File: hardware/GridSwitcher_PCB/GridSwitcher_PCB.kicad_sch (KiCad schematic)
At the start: 32 parts, among them IC5 ESDS304DBVR, IC8 ESDS304DBVR, IC9 ESDS304DBVR, J10 RS485, J11 Relays, J12 LEDs, J9 Display and Keypad, U1 74LS09, U2 74LS09, U33 SN65HVD11HD

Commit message: -enh made some progress on pcb/fp design
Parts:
- removed J10: RS485, symbol Connector:4P4C_Shielded
- removed J11: Relays, symbol Connector:Conn_01x16_Pin
- added J10: Temp Sensor RS485, Connector_JST:JST_PH_B4B-PH-K_1x04_P2.00mm_Vertical, symbol Connector:Conn_01x04_Pin
- added J13: UT_OUT, Connector_Dsub:DSUB-25_Female_Horizontal_P2.77x2.84mm_EdgePinOffset7.70mm_Housed_MountingHolesOffset9.12mm, symbol Connector:DB25_Plug_MountingHoles
- added R111, R112: DNP, Resistor_SMD:R_0603_1608Metric_Pad0.98x0.95mm_HandSolder, symbol Device:R
- H1: footprint (none) -> MountingHole:MountingHole_3.2mm_M3_ISO14580_Pad_TopBottom
- IC5, IC8, IC9: footprint (none) -> Library:SOT95P280X145-5N
- J5: renamed from J9; footprint (none) -> Connector_JST:JST_PHD_B12B-PHDSS_2x06_P2.00mm_Vertical
- J6: renamed from J12; footprint (none) -> Connector_JST:JST_PH_B6B-PH-K_1x06_P2.00mm_Vertical
- R103, R104, R105, R106, R2, R3, R4, R5, R81, R82, R83, R84, R85, R86, R87, R88, R89, R90, R91, R92: footprint (none) -> Resistor_SMD:R_0603_1608Metric_Pad0.98x0.95mm_HandSolder
- U1, U2: footprint (none) -> Package_SO:SO-14_5.3x10.2mm_P1.27mm
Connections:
- net +3V3: now also R112.2
- net +5V: now also R111.1
- net GND: now also J10.1 (Pin_1), J13.0 (PAD), J13.1, J13.13, J13.14 (P14), J13.16 (P16), J13.25 (P25), J13.3, J13.4
- net mosfet_drivers/MOS_10_OUT: now also J13.20 (P20)
- net mosfet_drivers/MOS_11_OUT: now also J13.7
- net mosfet_drivers/MOS_12_OUT: now also J13.19 (P19)
- net mosfet_drivers/MOS_13_OUT: now also J13.6
- net mosfet_drivers/MOS_14_OUT: now also J13.18 (P18)
- net mosfet_drivers/MOS_15_OUT: now also J13.5
- net mosfet_drivers/MOS_16_OUT: now also J13.17 (P17)
- net mosfet_drivers/MOS_1_OUT: now also J13.12
- net mosfet_drivers/MOS_2_OUT: now also J13.24 (P24)
- net mosfet_drivers/MOS_3_OUT: now also J13.11
- net mosfet_drivers/MOS_4_OUT: now also J13.23 (P23)
- net mosfet_drivers/MOS_5_OUT: now also J13.10
- net mosfet_drivers/MOS_6_OUT: now also J13.22 (P22)
- net mosfet_drivers/MOS_7_OUT: now also J13.9
- net mosfet_drivers/MOS_8_OUT: now also J13.21 (P21)
- net mosfet_drivers/MOS_9_OUT: now also J13.8
- net RS485_A: now reaches D22.1 (A1), U33.6 (A)
- net RS485_A: now also J10.2 (Pin_2), J13.2
- net RS485_B: now reaches D22.2 (A2), U33.7 (B)
- net RS485_B: now also J10.3 (Pin_3), J13.15 (P15)
- new net: J10.4 (Pin_4), R111.2, R112.1

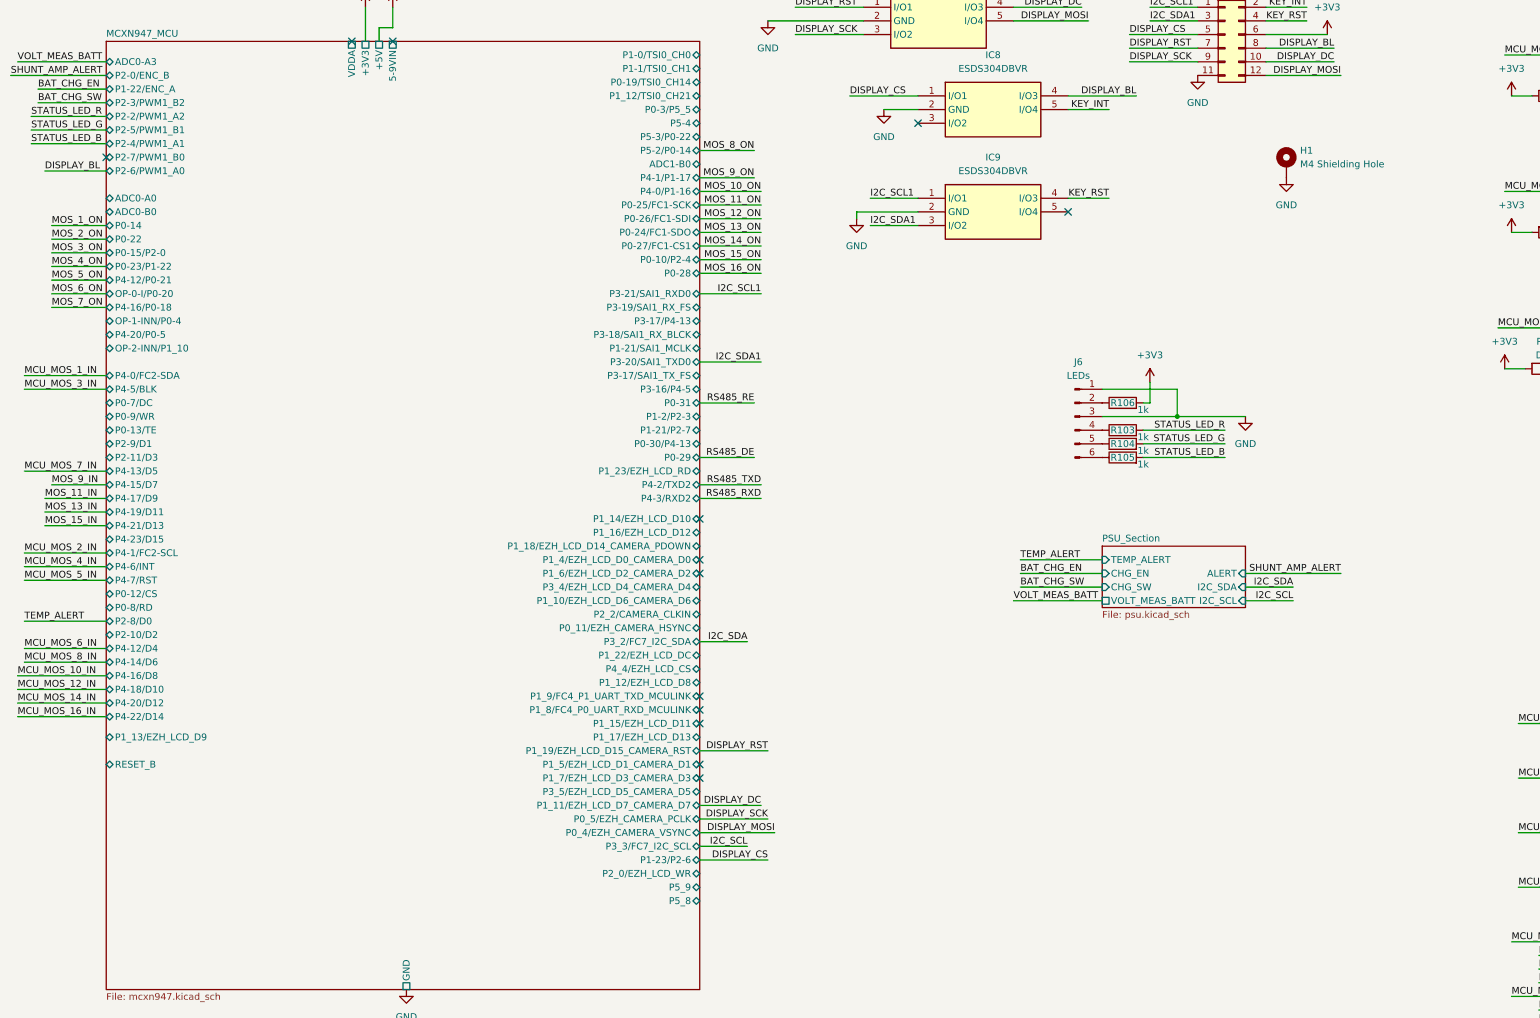
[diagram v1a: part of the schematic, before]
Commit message: -add some changes to schematic, tested the interfaces (uart, spi and i2c) with some test code
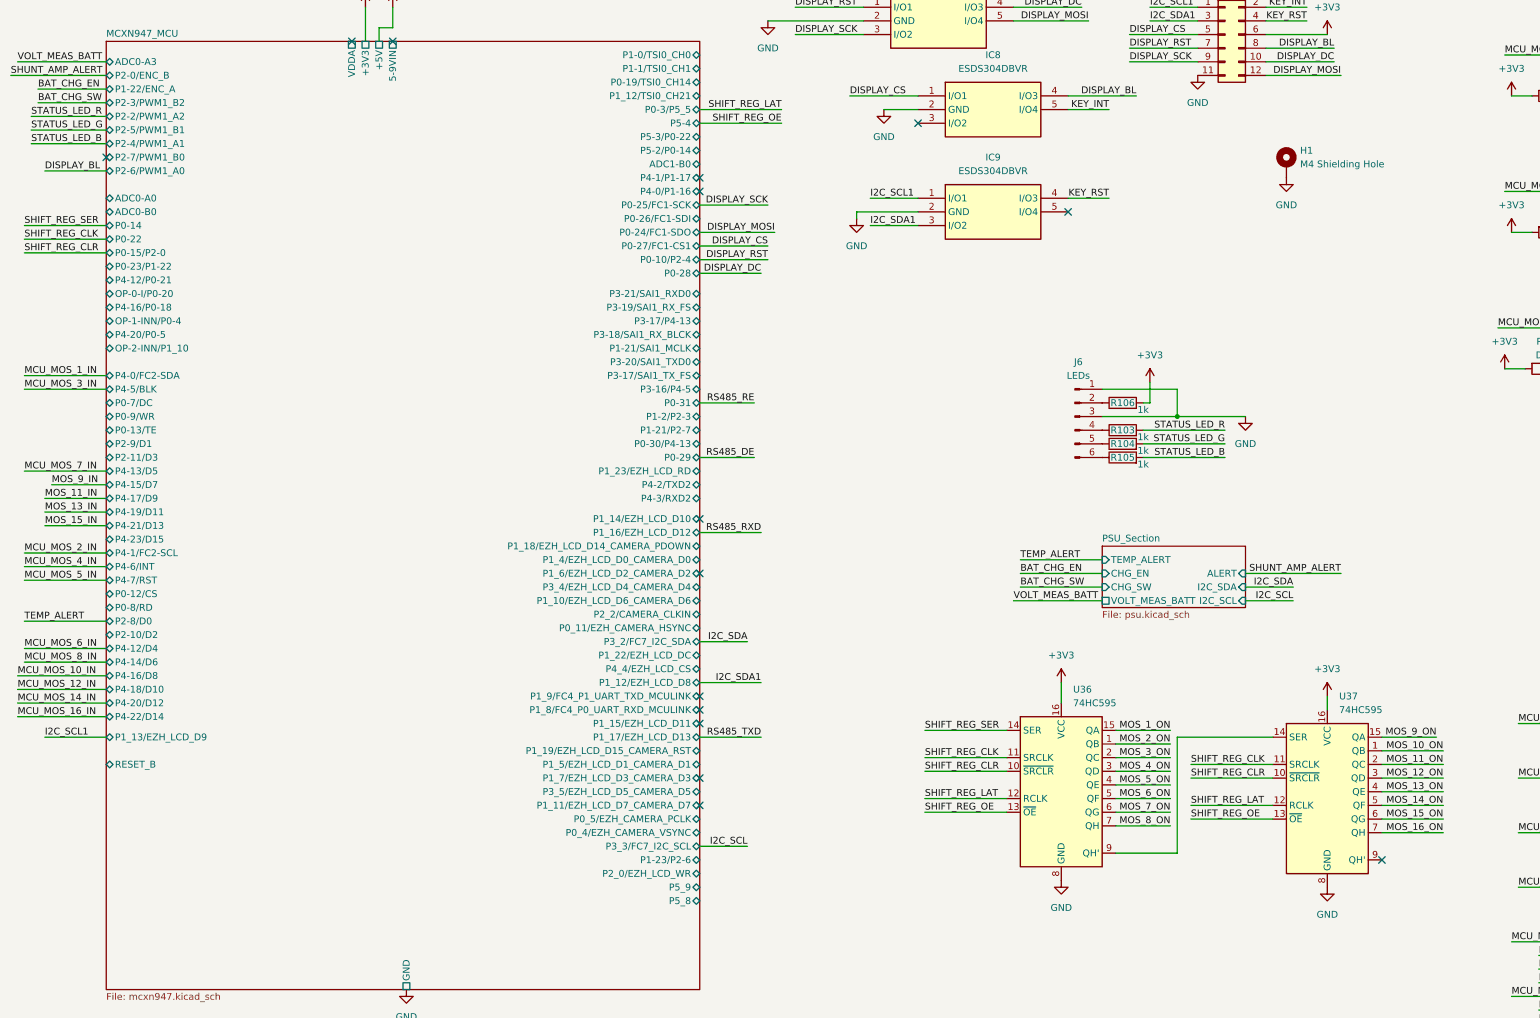
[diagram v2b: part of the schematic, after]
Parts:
- added U36, U37: 74HC595, symbol 74xx:74HC595
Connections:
- net +3V3: now also U36.16 (VCC), U37.16 (VCC)
- net GND: now also U36.8 (GND), U37.8 (GND)
- net MOS_10_ON: now also U37.1 (QB)
- net MOS_11_ON: now also U37.2 (QC)
- net MOS_12_ON: now also U37.3 (QD)
- net MOS_13_ON: now also U37.4 (QE)
- net MOS_14_ON: now also U37.5 (QF)
- net MOS_15_ON: now also U37.6 (QG)
- net MOS_16_ON: now also U37.7 (QH)
- net MOS_1_ON: now also U36.15 (QA)
- net MOS_2_ON: now also U36.1 (QB)
- net MOS_3_ON: now also U36.2 (QC)
- net MOS_4_ON: now also U36.3 (QD)
- net MOS_5_ON: now also U36.4 (QE)
- net MOS_6_ON: now also U36.5 (QF)
- net MOS_7_ON: now also U36.6 (QG)
- net MOS_8_ON: now also U36.7 (QH)
- net MOS_9_ON: now also U37.15 (QA)
- new net: U36.9 (QH'), U37.14 (SER)
- new net SHIFT_REG_CLK: U36.11 (SRCLK), U37.11 (SRCLK)
- new net SHIFT_REG_CLR: U36.10 (~{SRCLR}), U37.10 (~{SRCLR})
- new net SHIFT_REG_LAT: U36.12 (RCLK), U37.12 (RCLK)
- new net SHIFT_REG_OE: U36.13 (~{OE}), U37.13 (~{OE})
- new net SHIFT_REG_SER: U36.14 (SER)
- no-connect marks 13 -> 15

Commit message: -add some more pinning changes, add rts flow control for rs485
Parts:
- added H2, H3, H4, H5: MountingHole, MountingHole:MountingHole_3.2mm_M3, symbol Mechanical:MountingHole
- U36, U37: footprint (none) -> Package_SO:SOIC-16_3.9x9.9mm_P1.27mm
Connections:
- net RS485_DE: no longer U33.3 (DE)
- net RS485_RE: no longer U33.2 (~{RE})
- new net RS485_RTS: U33.2 (~{RE}), U33.3 (DE)
- no-connect marks 15 -> 17

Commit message: -enh final revision; ordered
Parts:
- added C10, C11, C12, C13, C14, C9: 100n, Capacitor_SMD:C_0603_1608Metric_Pad1.08x0.95mm_HandSolder, symbol Device:C_Small
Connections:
- net +3V3: now also C10.1, C11.1, C12.1, C13.1, C9.1
- net +5V: now also C14.1
- net DISPLAY_MOSI: now also IC5.1 (I/O1); no longer IC5.5 (I/O4)
- net DISPLAY_RST: now also IC5.5 (I/O4); no longer IC5.1 (I/O1)
- net GND: now also C10.2, C11.2, C12.2, C13.2, C14.2, C9.2
- net MCU_MOS_11_IN: now also U37.2 (QC)
- net MCU_MOS_13_IN: now also U2.12, U37.4 (QE); no longer U2.9
- net MCU_MOS_15_IN: now also U2.9, U37.6 (QG); no longer U2.12
- net MCU_MOS_1_IN: now also U36.15 (QA)
- net MCU_MOS_3_IN: now also U36.2 (QC)
- net MCU_MOS_5_IN: now also U1.12, U36.4 (QE); no longer U1.9
- net MCU_MOS_7_IN: now also U1.9, U36.6 (QG); no longer U1.12
- net MCU_MOS_9_IN: now also U37.15 (QA)
- net MOS_10_ON: no longer U37.1 (QB)
- net MOS_11_ON: no longer U37.2 (QC)
- net MOS_12_ON: no longer U37.3 (QD)
- net MOS_13_IN: now also U2.11; no longer U2.8
- net MOS_13_ON: no longer U37.4 (QE)
- net MOS_14_ON: no longer U37.5 (QF)
- net MOS_15_IN: now also U2.8; no longer U2.11
- net MOS_15_ON: no longer U37.6 (QG)
- net MOS_16_ON: no longer U37.7 (QH)
- net MOS_1_ON: no longer U36.15 (QA)
- net MOS_2_ON: no longer U36.1 (QB)
- net MOS_3_ON: no longer U36.2 (QC)
- net MOS_4_ON: no longer U36.3 (QD)
- net MOS_5_IN: now also U1.11; no longer U1.8
- net MOS_5_ON: no longer U36.4 (QE)
- net MOS_6_ON: no longer U36.5 (QF)
- net MOS_7_IN: now also U1.8; no longer U1.11
- net MOS_7_ON: no longer U36.6 (QG)
- net MOS_8_ON: no longer U36.7 (QH)
- net MOS_9_ON: no longer U37.15 (QA)
- net at R83.1, R84.2: now also U1.10; no longer U1.13
- net at R81.1, R82.2: now also U1.13; no longer U1.10
- net at R85.1, R89.2: now also U2.10; no longer U2.13
- net at R87.1, R91.2: now also U2.13; no longer U2.10
- new net MOS_10_IN: U37.1 (QB)
- new net MOS_12_IN: U37.3 (QD)
- new net MOS_14_IN: U37.5 (QF)
- new net MOS_16_IN: U37.7 (QH)
- new net MOS_2_IN: U36.1 (QB)
- new net MOS_4_IN: U36.3 (QD)
- new net MOS_6_IN: U36.5 (QF)
- new net MOS_8_IN: U36.7 (QH)
- no-connect marks 17 -> 36
